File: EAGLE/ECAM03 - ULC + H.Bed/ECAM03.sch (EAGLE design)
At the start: 38 parts, among them J1 MODULAR TOOL, J2 FAN1, J3 FAN2, J4 FAN3, J5 S4B-PH-SM4, J6 SSR, J7 RINGLIGHT, Q2 16MHz, U1 SP3485, U2 ATMEGA238, U3 MCP4725, U4 MAX31855, U5 NTR4003NT3G, U6 NOR(74LVC), U8 AP3032

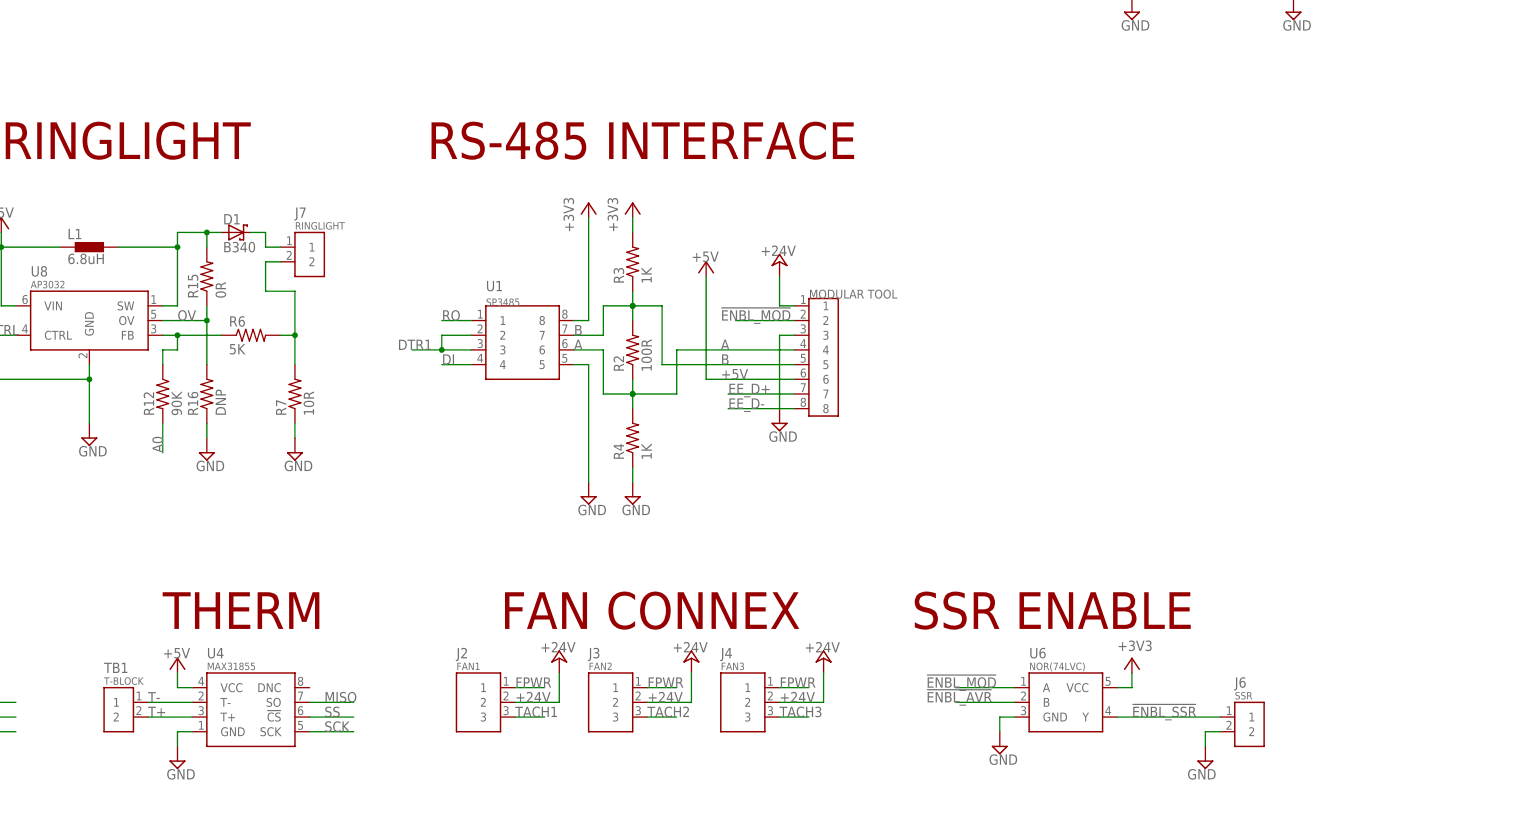
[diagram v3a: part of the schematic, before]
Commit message: Routed EFD01, ECAM03 boards. Modification needs to be made for hole/keepout in ECAM03. EMC03 X and Y sides routed. Will need to increase some trace widths.
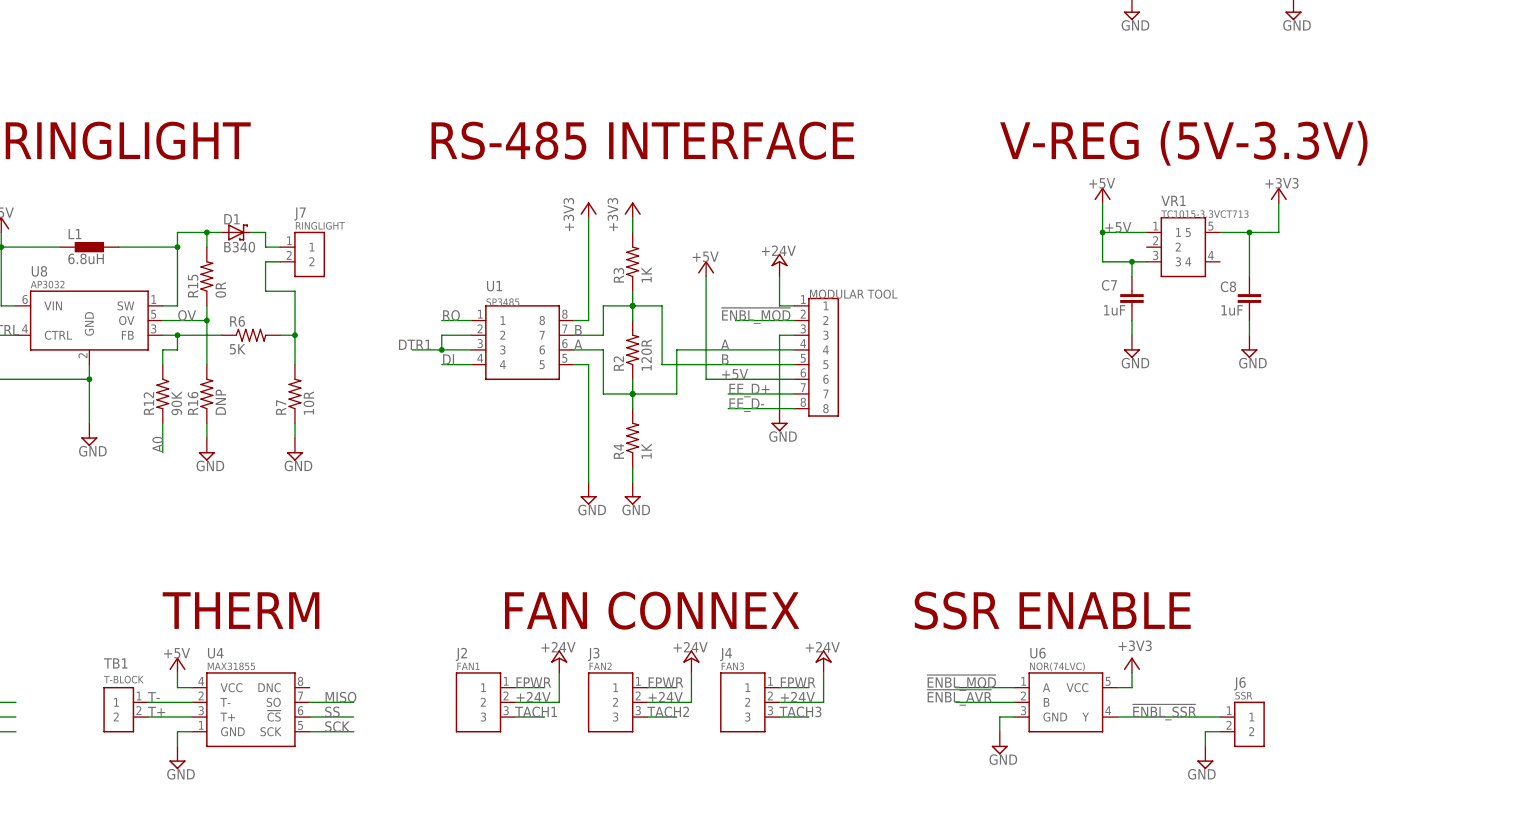
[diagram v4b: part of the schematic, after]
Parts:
- added C7, C8: 1uF, TinWhiskers:CPL-CAP-X5R-0603-1UF-50V
- added VR1: TC1015-3.3VCT713, TinWhiskers:CPL-REG-LIN-3.3V-0.1A
- R2: value 100R -> 120R; device TinWhiskers:CPL-RES-0603-100-0.1W -> TinWhiskers:CPL-RES-0603-120-0.1W
- TB1: device TinWhiskers:CPL-TBLK-SCR-2CKT-5.0MM -> TinWhiskers:CPL-TBLK-SCR-2CKT-5.0MM-OST
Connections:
- net +3V3: now also C8.2, VR1.5
- net +5V: now also C7.2, VR1.1, VR1.3
- net GND: now also C7.1, C8.1
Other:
- note added: "V-REG (5V-3.3V)"
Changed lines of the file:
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@@
 <part name="P+1" library="supply1" deviceset="+24V" device=""/>
 <part name="P+2" library="supply1" deviceset="+5V" device=""/>
-<part name="R2" library="TinWhiskers" deviceset="CPL-RES-0603-100-0.1W" device="" value="100R">
+<part name="R2" library="TinWhiskers" deviceset="CPL-RES-0603-120-0.1W" device="" value="120R">
 <attribute name="PARTNO" value="RC0603FR-07100RL"/>
 </part>
@@
 <part name="P+9" library="supply1" deviceset="+24V" device=""/>
 <part name="P+11" library="supply1" deviceset="+24V" device=""/>
-<part name="TB1" library="TinWhiskers" deviceset="CPL-TBLK-SCR-2CKT-5.0MM" device="" value="T-BLOCK"/>
+<part name="TB1" library="TinWhiskers" deviceset="CPL-TBLK-SCR-2CKT-5.0MM-OST" device="" value="T-BLOCK"/>
 <part name="SUPPLY8" library="TinWhiskers" deviceset="GND" device=""/>
 <part name="+3V1" library="supply1" deviceset="+3V3" device=""/>
@@
 <part name="SUPPLY16" library="TinWhiskers" deviceset="GND" device=""/>
 <part name="P+12" library="supply1" deviceset="+5V" device=""/>
+<part name="VR1" library="TinWhiskers" deviceset="CPL-REG-LIN-3.3V-0.1A" device="" value="TC1015-3.3VCT713">
+<attribute name="PARTNO" value="TC1015-3.3VCT713"/>
+</part>
+<part name="C7" library="TinWhiskers" deviceset="CPL-CAP-X5R-0603-1UF-50V" device="" value="1uF">
+<attribute name="PARTNO" value="UMK107AB7105KA-T"/>
+</part>
+<part name="C8" library="TinWhiskers" deviceset="CPL-CAP-X5R-0603-1UF-50V" device="" value="1uF">
+<attribute name="PARTNO" value="UMK107AB7105KA-T"/>
+</part>
+<part name="SUPPLY22" library="TinWhiskers" deviceset="GND" device=""/>
+<part name="SUPPLY23" library="TinWhiskers" deviceset="GND" device=""/>
+<part name="P+4" library="supply1" deviceset="+5V" device=""/>
+<part name="+3V4" library="supply1" deviceset="+3V3" device=""/>
 </parts>
 <sheets>
@@
 <text x="17.78" y="68.58" size="6.35" layer="94" ratio="10">FAN SWITCH</text>
 <text x="281.94" y="68.58" size="6.35" layer="94" ratio="10">SSR ENABLE</text>
+<text x="297.18" y="149.86" size="6.35" layer="94" ratio="10">V-REG (5V-3.3V)</text>
 </plain>
 <instances>
@@
 <attribute name="VALUE" x="263.398" y="64.516" size="1.778" layer="96"/>
 </instance>
-<instance part="TB1" gate="G$1" x="144.78" y="55.88" smashed="yes" rot="MR0">
-<attribute name="NAME" x="142.24" y="60.96" size="1.778" layer="95" font="vector" ratio="12"/>
-<attribute name="VALUE" x="142.24" y="58.928" size="1.27" layer="96" font="vector" ratio="10"/>
+<instance part="TB1" gate="G$1" x="147.32" y="53.34" smashed="yes">
+<attribute name="NAME" x="142.24" y="63.5" size="1.778" layer="95" font="vector" ratio="12" rot="MR180"/>
+<attribute name="VALUE" x="142.24" y="60.452" size="1.27" layer="96" font="vector" ratio="10" rot="MR180"/>
 </instance>
 <instance part="SUPPLY8" gate="GND" x="297.18" y="48.26"/>
@@
 <instance part="P+12" gate="1" x="58.42" y="137.16" smashed="yes">
 <attribute name="VALUE" x="55.88" y="137.16" size="1.778" layer="96"/>
+</instance>
+<instance part="VR1" gate="G$1" x="332.74" y="132.08" smashed="yes">
+<attribute name="NAME" x="325.12" y="141.732" size="1.778" layer="95" font="vector" ratio="12"/>
+<attribute name="VALUE" x="325.12" y="139.7" size="1.27" layer="95" font="vector" ratio="10"/>
+<attribute name="PARTNO" x="332.74" y="132.08" size="1.778" layer="96" display="off"/>
+</instance>
+<instance part="C7" gate="G$1" x="320.04" y="127" smashed="yes" rot="R90">
+<attribute name="NAME" x="314.706" y="127.127" size="1.778" layer="95"/>
+<attribute name="VALUE" x="314.96" y="122.809" size="1.778" layer="96"/>
+<attribute name="PARTNO" x="320.04" y="127" size="1.778" layer="96" display="off"/>
+</instance>
+<instance part="C8" gate="G$1" x="340.36" y="127" smashed="yes" rot="R90">
+<attribute name="NAME" x="335.28" y="126.873" size="1.778" layer="95"/>
+<attribute name="VALUE" x="335.28" y="122.809" size="1.778" layer="96"/>
+<attribute name="PARTNO" x="340.36" y="127" size="1.778" layer="96" display="off"/>
+</instance>
+<instance part="SUPPLY22" gate="GND" x="320.04" y="116.84"/>
+<instance part="SUPPLY23" gate="GND" x="340.36" y="116.84"/>
+<instance part="P+4" gate="1" x="314.96" y="144.78" smashed="yes">
+<attribute name="VALUE" x="312.42" y="144.78" size="1.778" layer="96"/>
+</instance>
+<instance part="+3V4" gate="G$1" x="345.44" y="144.78" smashed="yes">
+<attribute name="VALUE" x="342.9" y="144.78" size="1.778" layer="96"/>
 </instance>
 </instances>
@@
 <wire x1="175.26" y1="101.6" x2="175.26" y2="104.14" width="0.1524" layer="91"/>
 </segment>
+<segment>
+<pinref part="C7" gate="G$1" pin="1"/>
+<pinref part="SUPPLY22" gate="GND" pin="GND"/>
+<wire x1="320.04" y1="119.38" x2="320.04" y2="121.92" width="0.1524" layer="91"/>
+</segment>
+<segment>
+<pinref part="C8" gate="G$1" pin="1"/>
+<pinref part="SUPPLY23" gate="GND" pin="GND"/>
+<wire x1="340.36" y1="121.92" x2="340.36" y2="119.38" width="0.1524" layer="91"/>
+</segment>
 </net>
 <net name="+5V" class="0">
@@
 <wire x1="58.42" y1="121.92" x2="58.42" y2="134.62" width="0.1524" layer="91"/>
 <pinref part="P+12" gate="1" pin="+5V"/>
+</segment>
+<segment>
+<pinref part="VR1" gate="G$1" pin="1"/>
+<wire x1="314.96" y1="137.16" x2="322.58" y2="137.16" width="0.1524" layer="91"/>
+<wire x1="314.96" y1="137.16" x2="314.96" y2="132.08" width="0.1524" layer="91"/>
+<pinref part="VR1" gate="G$1" pin="3"/>
+<wire x1="314.96" y1="132.08" x2="320.04" y2="132.08" width="0.1524" layer="91"/>
+<label x="315.214" y="137.16" size="1.778" layer="95"/>
+<pinref part="P+4" gate="1" pin="+5V"/>
+<wire x1="320.04" y1="132.08" x2="322.58" y2="132.08" width="0.1524" layer="91"/>
+<wire x1="314.96" y1="142.24" x2="314.96" y2="137.16" width="0.1524" layer="91"/>
+<junction x="314.96" y="137.16"/>
+<pinref part="C7" gate="G$1" pin="2"/>
+<wire x1="320.04" y1="132.08" x2="320.04" y2="129.54" width="0.1524" layer="91"/>
+<junction x="320.04" y="132.08"/>
 </segment>
 </net>
@@
 <pinref part="U6" gate="G$1" pin="VCC"/>
 </segment>
-</net>
+<segment>
+<pinref part="VR1" gate="G$1" pin="5"/>
+<pinref part="C8" gate="G$1" pin="2"/>
+<wire x1="335.28" y1="137.16" x2="340.36" y2="137.16" width="0.1524" layer="91"/>
+<wire x1="340.36" y1="137.16" x2="340.36" y2="129.54" width="0.1524" layer="91"/>
+<wire x1="340.36" y1="137.16" x2="345.44" y2="137.16" width="0.1524" layer="91"/>
+<wire x1="345.44" y1="137.16" x2="345.44" y2="142.24" width="0.1524" layer="91"/>
+<junction x="340.36" y="137.16"/>
+<pinref part="+3V4" gate="G$1" pin="+3V3"/>
+</segment>
+</net>

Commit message: Updated all boards to include changes for production
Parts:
- J2, J3, J4: device TinWhiskers:CPL-CON-HEADER-0.1IN-3P-M -> FirePick:CONN-RECT-3PINMOLEX-KK
- J5: device TinWhiskers:CPL-CON-JST-2.0MM-4P-M-SMT-RA -> TinWhiskers:CPL-CON-JST-2.0MM-4P-M-SMT-VRT
- J7: device TinWhiskers:CPL-CON-JST-2.0MM-2P-M-SMT-RA -> TinWhiskers:CPL-CON-JST-2.0MM-5P-SMT-VRT
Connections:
- net +5V: now also J7.5
- net GND: now also J7.3
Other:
- moved on the sheet: J2, J3, J4
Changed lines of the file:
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@@
 <part name="R16" library="TinWhiskers" deviceset="CPL-RES-0603-0-0.1W" device="" value="DNP"/>
 <part name="SUPPLY26" library="TinWhiskers" deviceset="GND" device=""/>
-<part name="J7" library="TinWhiskers" deviceset="CPL-CON-JST-2.0MM-2P-M-SMT-RA" device="" value="RINGLIGHT"/>
-<part name="J5" library="TinWhiskers" deviceset="CPL-CON-JST-2.0MM-4P-M-SMT-RA" device="" value="S4B-PH-SM4">
+<part name="J5" library="TinWhiskers" deviceset="CPL-CON-JST-2.0MM-4P-M-SMT-VRT" device="" value="S4B-PH-SM4">
 <attribute name="PARTNO" value="S4B-PH-SM4-TB(LF)(SN)"/>
 </part>
@@
 <part name="SUPPLY6" library="TinWhiskers" deviceset="GND" device=""/>
 <part name="P+6" library="supply1" deviceset="+5V" device=""/>
-<part name="J2" library="TinWhiskers" deviceset="CPL-CON-HEADER-0.1IN-3P-M" device="" value="FAN1"/>
-<part name="J3" library="TinWhiskers" deviceset="CPL-CON-HEADER-0.1IN-3P-M" device="" value="FAN2"/>
-<part name="J4" library="TinWhiskers" deviceset="CPL-CON-HEADER-0.1IN-3P-M" device="" value="FAN3"/>
+<part name="J2" library="FirePick" deviceset="CONN-RECT-3PIN" device="MOLEX-KK" value="FAN1"/>
+<part name="J3" library="FirePick" deviceset="CONN-RECT-3PIN" device="MOLEX-KK" value="FAN2"/>
+<part name="J4" library="FirePick" deviceset="CONN-RECT-3PIN" device="MOLEX-KK" value="FAN3"/>
 <part name="U5" library="TinWhiskers" deviceset="CPL-MOSFET-NCH-SOT23" device="" value="NTR4003NT3G"/>
 <part name="SUPPLY7" library="TinWhiskers" deviceset="GND" device=""/>
@@
 <part name="P+4" library="supply1" deviceset="+5V" device=""/>
 <part name="+3V4" library="supply1" deviceset="+3V3" device=""/>
+<part name="J7" library="TinWhiskers" deviceset="CPL-CON-JST-2.0MM-5P-SMT-VRT" device="" value="RINGLIGHT"/>
+<part name="SUPPLY15" library="TinWhiskers" deviceset="GND" device=""/>
+<part name="P+13" library="supply1" deviceset="+5V" device=""/>
 </parts>
 <sheets>
@@
 <attribute name="VALUE" x="158.115" y="95.885" size="1.778" layer="96"/>
 </instance>
-<instance part="J7" gate="G$1" x="175.26" y="132.08" smashed="yes" rot="MR0">
-<attribute name="NAME" x="175.26" y="139.7" size="1.778" layer="95" font="vector" ratio="12"/>
-<attribute name="VALUE" x="175.26" y="137.668" size="1.27" layer="96" font="vector" ratio="10"/>
-</instance>
 <instance part="J5" gate="G$1" x="66.04" y="127" smashed="yes" rot="MR0">
 <attribute name="NAME" x="66.04" y="134.62" size="1.778" layer="95" font="vector" ratio="12"/>
@@
 <instance part="+3V4" gate="G$1" x="345.44" y="144.78" smashed="yes">
 <attribute name="VALUE" x="342.9" y="144.78" size="1.778" layer="96"/>
+</instance>
+<instance part="J7" gate="G$1" x="185.42" y="129.54" rot="MR0"/>
+<instance part="SUPPLY15" gate="GND" x="180.34" y="116.84" smashed="yes">
+<attribute name="VALUE" x="178.435" y="113.665" size="1.778" layer="96"/>
+</instance>
+<instance part="P+13" gate="1" x="177.8" y="142.24" smashed="yes">
+<attribute name="VALUE" x="175.26" y="142.24" size="1.778" layer="96"/>
 </instance>
 </instances>
@@
 <wire x1="340.36" y1="121.92" x2="340.36" y2="119.38" width="0.1524" layer="91"/>
 </segment>
+<segment>
+<pinref part="J7" gate="G$1" pin="3"/>
+<wire x1="182.88" y1="129.54" x2="180.34" y2="129.54" width="0.1524" layer="91"/>
+<pinref part="SUPPLY15" gate="GND" pin="GND"/>
+<wire x1="180.34" y1="129.54" x2="180.34" y2="119.38" width="0.1524" layer="91"/>
+</segment>
 </net>
 <net name="+5V" class="0">
@@
 <wire x1="320.04" y1="132.08" x2="320.04" y2="129.54" width="0.1524" layer="91"/>
 <junction x="320.04" y="132.08"/>
+</segment>
+<segment>
+<pinref part="J7" gate="G$1" pin="5"/>
+<wire x1="182.88" y1="124.46" x2="177.8" y2="124.46" width="0.1524" layer="91"/>
+<wire x1="177.8" y1="124.46" x2="177.8" y2="139.7" width="0.1524" layer="91"/>
+<pinref part="P+13" gate="1" pin="+5V"/>
 </segment>
 </net>
@@
 <wire x1="167.64" y1="137.16" x2="170.18" y2="137.16" width="0.1524" layer="91"/>
 <wire x1="170.18" y1="137.16" x2="170.18" y2="134.62" width="0.1524" layer="91"/>
-<wire x1="170.18" y1="134.62" x2="172.72" y2="134.62" width="0.1524" layer="91"/>
+<wire x1="170.18" y1="134.62" x2="182.88" y2="134.62" width="0.1524" layer="91"/>
 <pinref part="J7" gate="G$1" pin="1"/>
 </segment>
@@
 </segment>
 </net>
-<net name="N$3" class="0">
-<segment>
-<pinref part="J7" gate="G$1" pin="2"/>
-<wire x1="172.72" y1="132.08" x2="170.18" y2="132.08" width="0.1524" layer="91"/>
-<wire x1="170.18" y1="132.08" x2="170.18" y2="127" width="0.1524" layer="91"/>
-<wire x1="170.18" y1="127" x2="175.26" y2="127" width="0.1524" layer="91"/>
-<wire x1="175.26" y1="127" x2="175.26" y2="119.38" width="0.1524" layer="91"/>
-<pinref part="R7" gate="G$1" pin="2"/>
-<pinref part="R6" gate="G$1" pin="2"/>
-<wire x1="175.26" y1="119.38" x2="175.26" y2="114.3" width="0.1524" layer="91"/>
-<wire x1="172.72" y1="119.38" x2="175.26" y2="119.38" width="0.1524" layer="91"/>
-<junction x="175.26" y="119.38"/>
-</segment>
-</net>
 <net name="N$4" class="0">
 <segment>
@@
 </segment>
 </net>
+<net name="N$6" class="0">
+<segment>
+<pinref part="R7" gate="G$1" pin="2"/>
+<pinref part="R6" gate="G$1" pin="2"/>
+<wire x1="175.26" y1="119.38" x2="175.26" y2="114.3" width="0.1524" layer="91"/>
+<wire x1="172.72" y1="119.38" x2="175.26" y2="119.38" width="0.1524" layer="91"/>
+<wire x1="175.26" y1="119.38" x2="175.26" y2="121.92" width="0.1524" layer="91"/>
+<junction x="175.26" y="119.38"/>
+<wire x1="175.26" y1="121.92" x2="170.18" y2="121.92" width="0.1524" layer="91"/>
+<wire x1="182.88" y1="132.08" x2="170.18" y2="132.08" width="0.1524" layer="91"/>
+<pinref part="J7" gate="G$1" pin="2"/>
+<wire x1="170.18" y1="121.92" x2="170.18" y2="132.08" width="0.1524" layer="91"/>
+</segment>
+</net>
